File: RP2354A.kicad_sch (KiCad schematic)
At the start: 26 parts, among them SW1 Button, SW2 Button, U1 RP2354A, U2 ABM8-272-T3

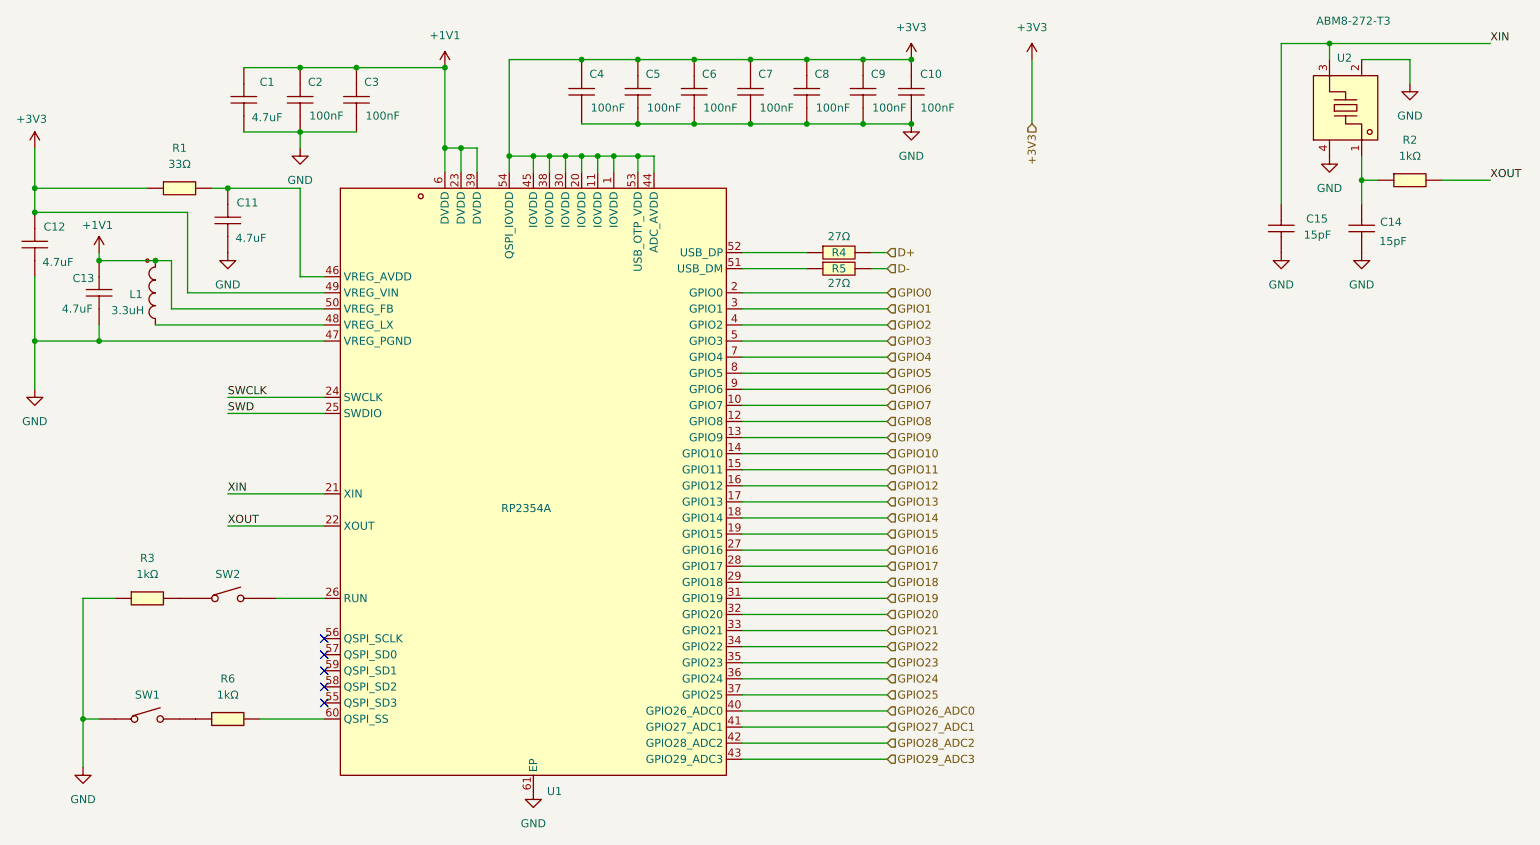
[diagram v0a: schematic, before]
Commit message: switched to RP2350A and added flash chip due to parts shortage
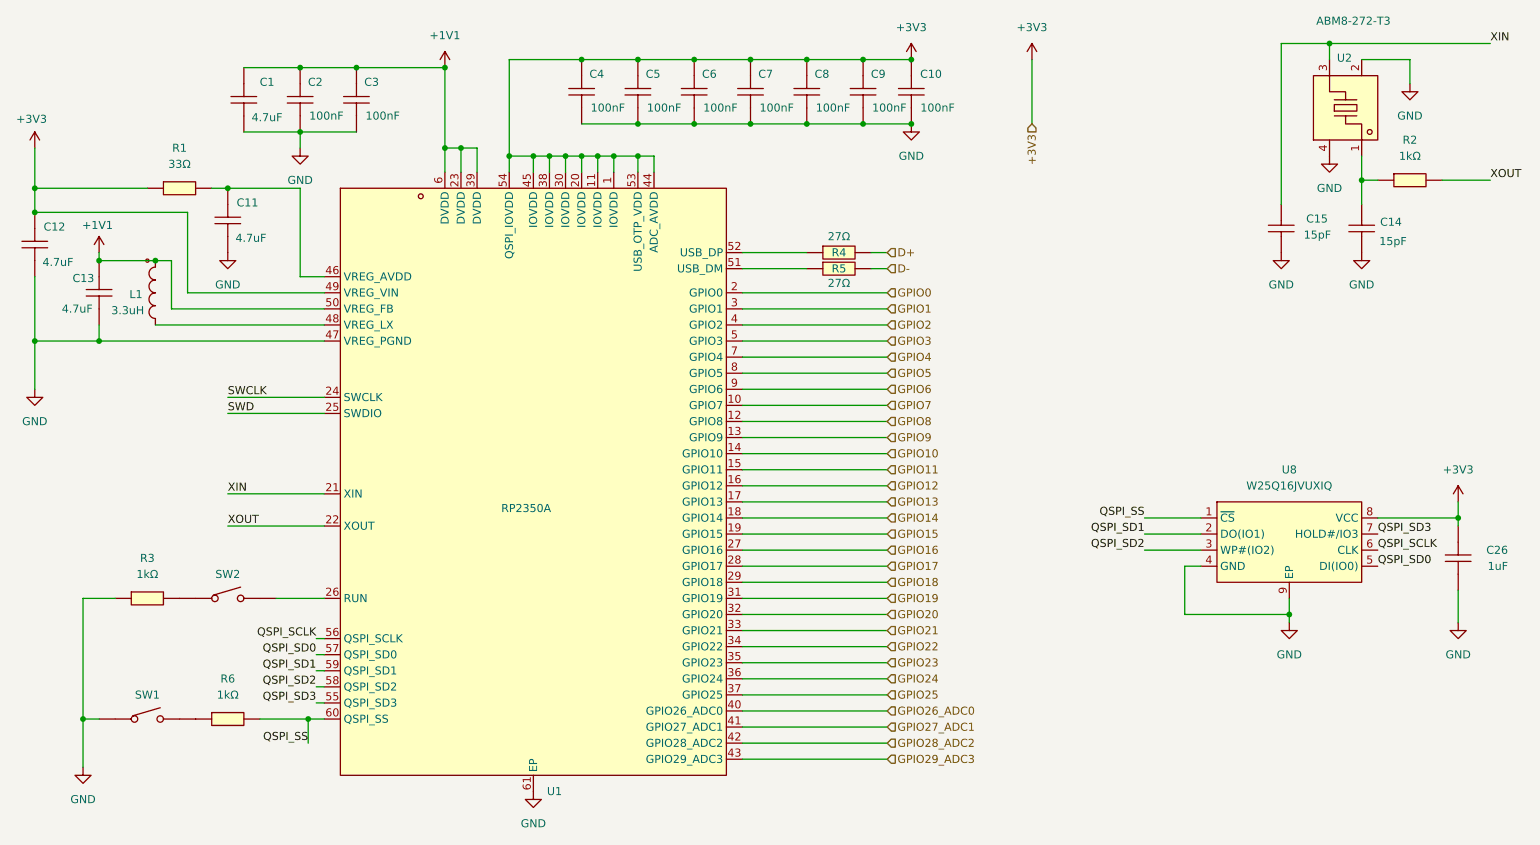
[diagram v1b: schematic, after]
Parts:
- added C26: 1uF, Capacitors:C0402, symbol Capacitors:1uF_C0402
- added U8: W25Q16JVUXIQ, Other:USON-8_L3.0-W2.0-P0.50-BL-EP, symbol Other:W25Q16JVUXIQ
- U1: value RP2354A -> RP2350A; LCSC Part C41378174 -> C42411118
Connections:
- net +3V3: now also C26.2, U8.8 (VCC)
- net GND: now also C26.1, U8.4 (GND), U8.9 (EP)
- net QSPI_SS: now reaches R6.2, U1.60 (QSPI_SS)
- net QSPI_SS: now also U8.1 (~{CS})
- net QSPI_SD3: now reaches U1.55 (QSPI_SD3)
- net QSPI_SD3: now also U8.7 (HOLD#/IO3)
- net QSPI_SCLK: now reaches U1.56 (QSPI_SCLK)
- net QSPI_SCLK: now also U8.6 (CLK)
- net QSPI_SD0: now reaches U1.57 (QSPI_SD0)
- net QSPI_SD0: now also U8.5 (DI(IO0))
- net QSPI_SD2: now reaches U1.58 (QSPI_SD2)
- net QSPI_SD2: now also U8.3 (WP#(IO2))
- net QSPI_SD1: now reaches U1.59 (QSPI_SD1)
- net QSPI_SD1: now also U8.2 (DO(IO1))
- no-connect marks 5 -> 0

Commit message: Final manufactured version
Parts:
- removed C26: 1uF, Capacitors:C0402, symbol Capacitors:1uF_C0402
- removed U8: W25Q16JVUXIQ, Other:USON-8_L3.0-W2.0-P0.50-BL-EP, symbol Other:W25Q16JVUXIQ
- U1: value RP2350A -> RP2354A; LCSC Part C42411118 -> C41378174
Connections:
- net QSPI_SCLK: no longer names the net of U1.56 (QSPI_SCLK)
- net QSPI_SD0: no longer names the net of U1.57 (QSPI_SD0)
- net QSPI_SD1: no longer names the net of U1.59 (QSPI_SD1)
- net QSPI_SD2: no longer names the net of U1.58 (QSPI_SD2)
- net QSPI_SD3: no longer names the net of U1.55 (QSPI_SD3)
- net QSPI_SS: no longer names the net of R6.2, U1.60 (QSPI_SS)
- no-connect marks 0 -> 5
